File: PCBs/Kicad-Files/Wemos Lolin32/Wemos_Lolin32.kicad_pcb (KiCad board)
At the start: 2 copper layers, 55.8 x 92.7 mm, 27 parts, among them J1 Neopixel, J10 RFID2, J11 Battery, J12 toLolin, J13 Reset, J2 to-Headphone, J3 RotEncoder, J4 Next-Bt, J5 RFID1, J6 Prev-Bt, J7 MAX98357a, J8 uSD-Reader, J9 PPlay-Bt, Q1 IRF530NPbF, Q2 NDP6020P, U1 Wemos Lolin32

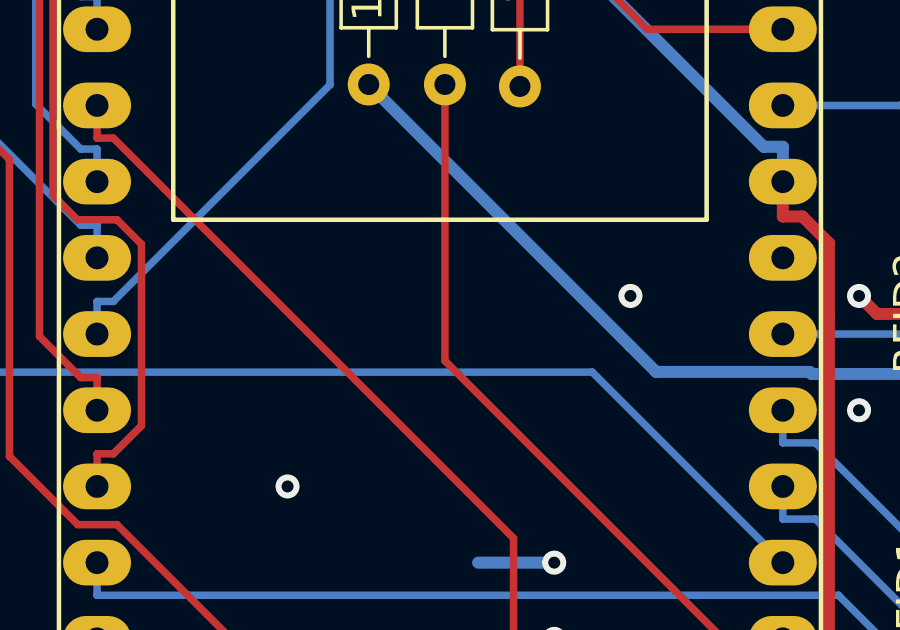
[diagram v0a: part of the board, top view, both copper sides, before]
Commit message: KiCad-Files umbenennen: Lolin32
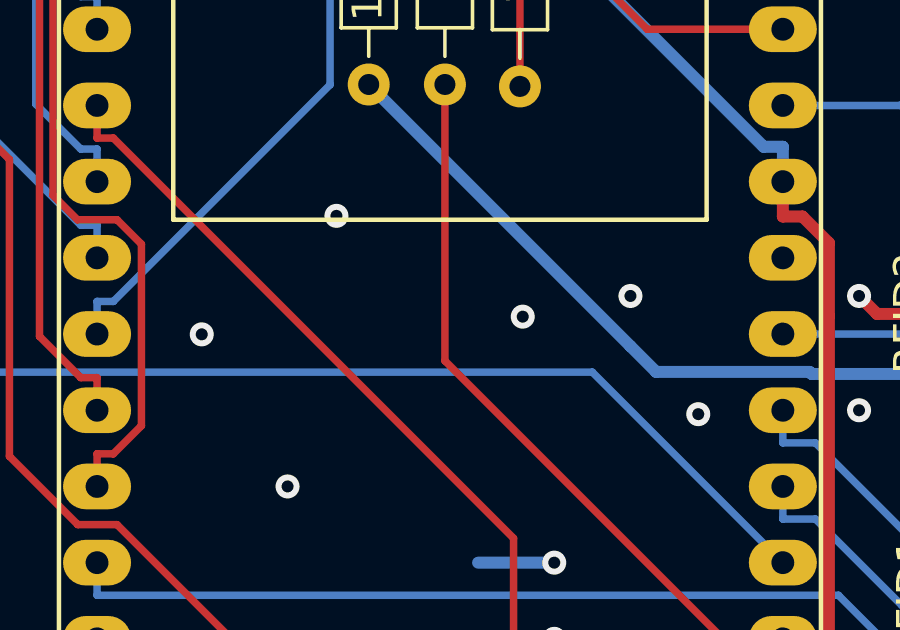
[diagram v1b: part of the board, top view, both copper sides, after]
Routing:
- net GND: vias 20 -> 24
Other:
- board text added: "ESPuino Lolin32 3.3V rev2"
- board text removed: "Tonuino Lolin32 3.3V rev2"
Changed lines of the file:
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@@
-(kicad_pcb (version 20171130) (host pcbnew "(5.1.8-0-10_14)")
+(kicad_pcb (version 20171130) (host pcbnew 5.1.5+dfsg1-2build2)
   (general
     (thickness 1.6)
     (drawings 44)
-    (tracks 302)
+    (tracks 306)
     (zones 0)
     (modules 27)
@@
   (gr_line (start 95.25 114.3) (end 151 114.3) (layer Edge.Cuts) (width 0.15))
   (gr_line (start 95.25 21.59) (end 151 21.59) (layer Edge.Cuts) (width 0.15))
-  (gr_text "Tonuino Lolin32 3.3V rev2" (at 122.555 111.125) (layer B.SilkS)
+  (gr_text "ESPuino Lolin32 3.3V rev2" (at 119.01 112.38) (layer B.SilkS)
     (effects (font (size 1.5 1.5) (thickness 0.3)) (justify mirror))
   )
@@
   (segment (start 136.49 69.18) (end 135.89 68.58) (width 0.4) (layer F.Cu) (net 34))
   (segment (start 141.8 69.18) (end 136.49 69.18) (width 0.4) (layer F.Cu) (net 34))
+  (via (at 118.47 65.91) (size 0.8) (drill 0.4) (layers F.Cu B.Cu) (net 34))
+  (via (at 124.68 69.27) (size 0.8) (drill 0.4) (layers F.Cu B.Cu) (net 34))
+  (via (at 113.98 69.86) (size 0.8) (drill 0.4) (layers F.Cu B.Cu) (net 34))
+  (via (at 130.53 72.52) (size 0.8) (drill 0.4) (layers F.Cu B.Cu) (net 34))
   (segment (start 121.285 38.1) (end 121.285 39.2753) (width 0.25) (layer F.Cu) (net 35) (status 10))
   (segment (start 119.546 53.9111) (end 119.546 41.0143) (width 0.25) (layer F.Cu) (net 35) (status 10))
